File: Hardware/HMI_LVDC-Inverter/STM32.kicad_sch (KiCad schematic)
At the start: 22 parts, among them SW1 SW_MEC_5E, U4 STM32F103C8Tx, Y1 Crystal 8MHz

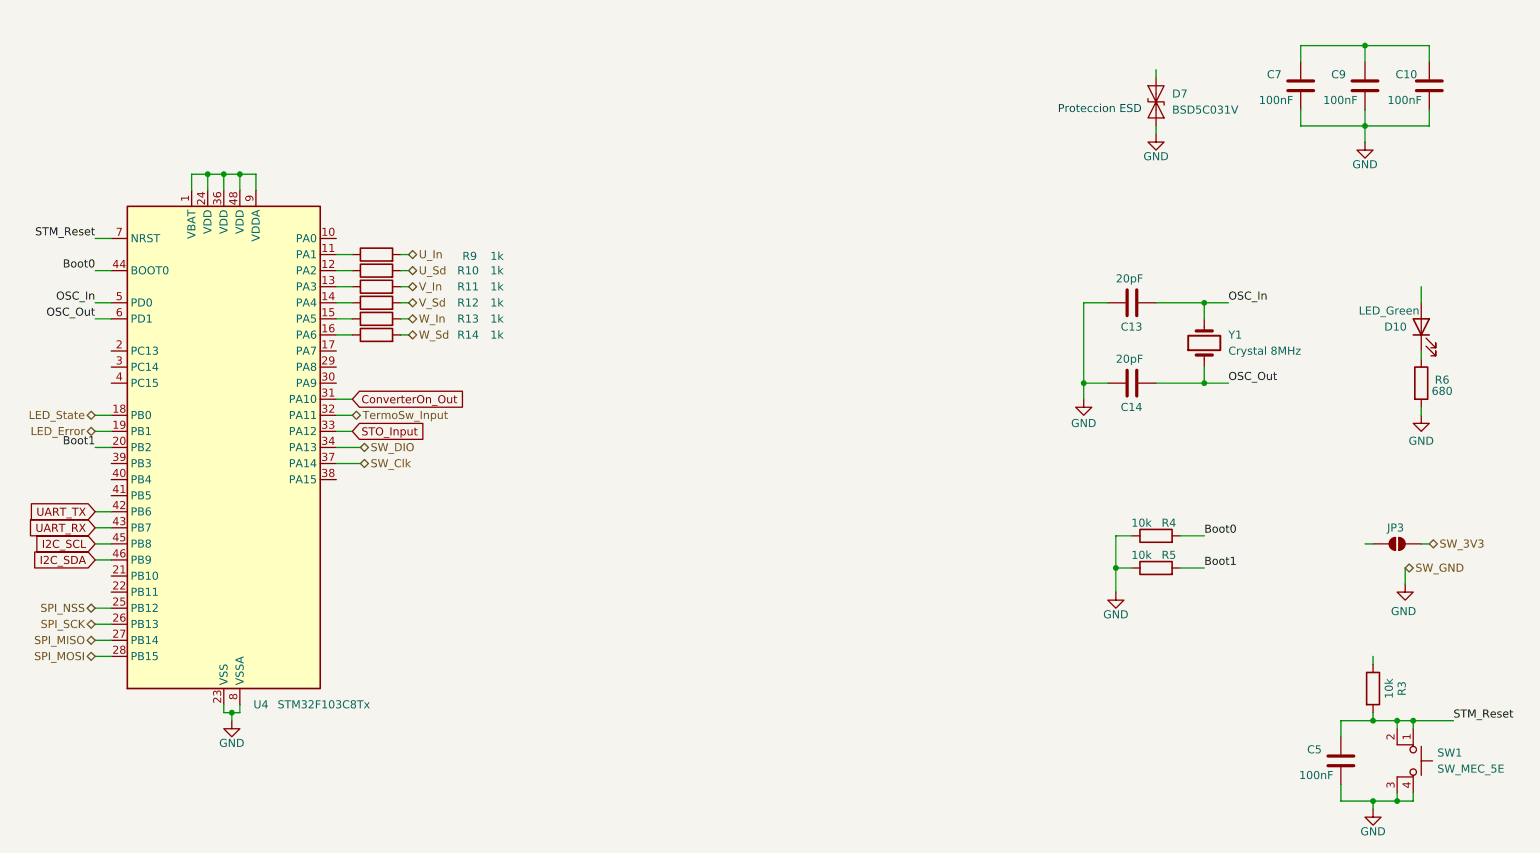
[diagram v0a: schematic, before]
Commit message: Terminado todo el conexionado eléctrico esquemático
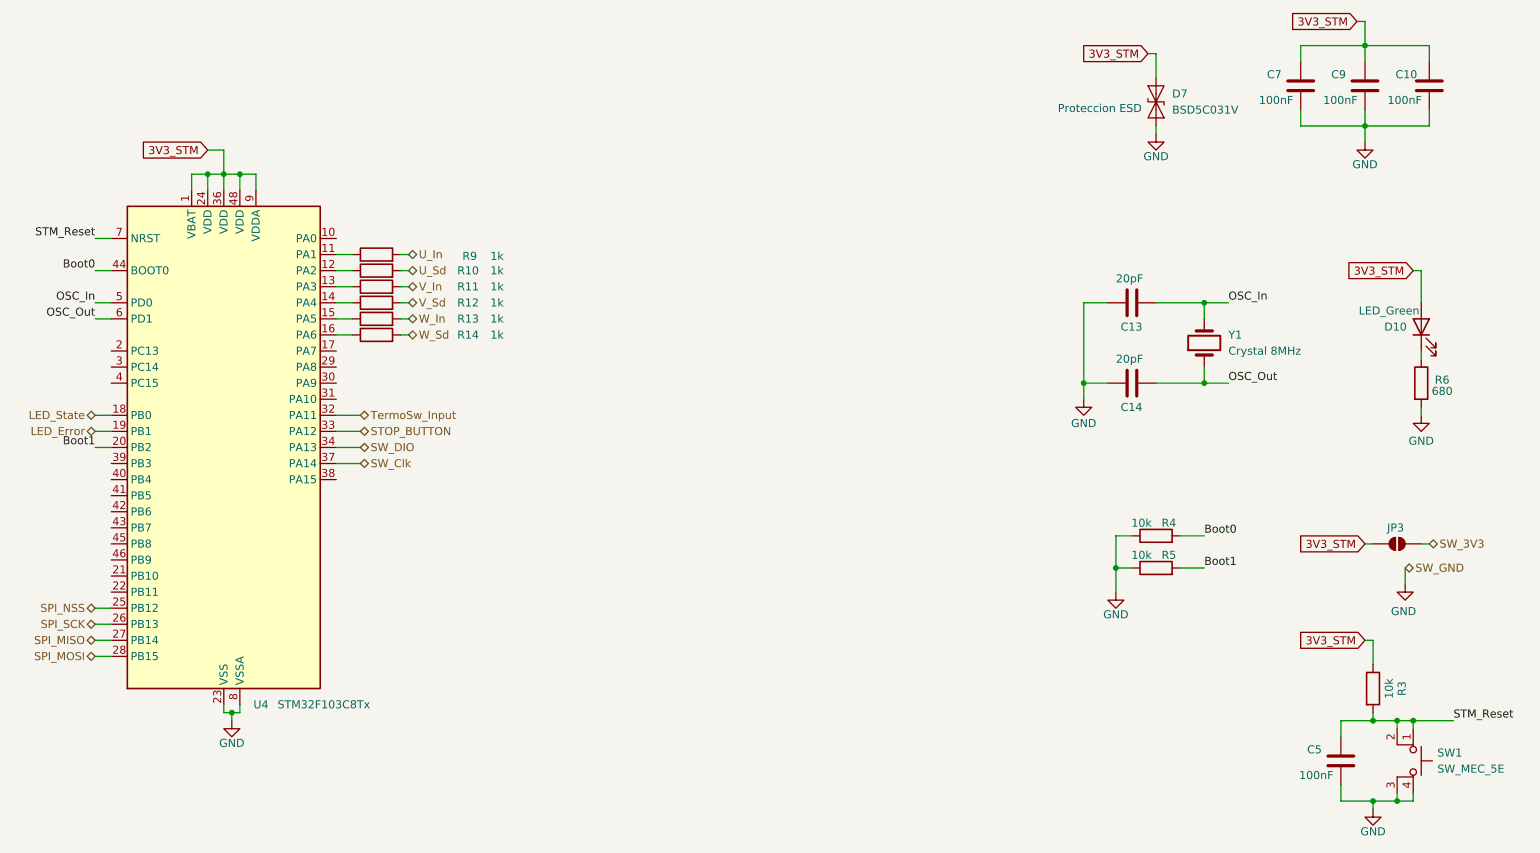
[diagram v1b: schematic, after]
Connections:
- net 3V3_STM: now reaches R3.1
- net 3V3_STM: now also C10.1, C7.1, C9.1, D10.2 (A), D7.2 (A2), JP3.1 (A), U4.1 (VBAT), U4.24 (VDD), U4.36 (VDD), U4.48 (VDD), U4.9 (VDDA)
- net ConverterOn_Out: no longer names the net of U4.31 (PA10)
- net I2C_SCL: no longer names the net of U4.45 (PB8)
- net I2C_SDA: no longer names the net of U4.46 (PB9)
- net STO_Input renamed STOP_BUTTON
- net UART_RX: no longer names the net of U4.43 (PB7)
- net UART_TX: no longer names the net of U4.42 (PB6)
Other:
- company: (none) -> Andrenacci - Carra
- title: (none) -> Variador de frecuencia LVDC

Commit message: Agregado de los componentes con links de compra en KiCAD a excepción de los conectores
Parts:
- removed SW1: SW_MEC_5E, TatilSwitch:Vertical SPST SMD Tactile Switches, symbol Switch:SW_MEC_5E
- added SW1: SolderJumper_2_Open, Jumper:SolderJumper-2_P1.3mm_Open_RoundedPad1.0x1.5mm, symbol Jumper:SolderJumper_2_Open
- C1: renamed from C7; Compra (none) -> https://www.lcsc.com/product-detail/C14663.html; Footprint checked (none) -> Yes; Manufacturer (none) -> Yagueo; Price (none) -> 0.24; Symbol checked (none) -> Yes
- C2: renamed from C9; Compra (none) -> https://www.lcsc.com/product-detail/C14663.html; Footprint checked (none) -> Yes; Manufacturer (none) -> Yagueo; Price (none) -> 0.24; Symbol checked (none) -> Yes
- C3: renamed from C10; Compra (none) -> https://www.lcsc.com/product-detail/C14663.html; Footprint checked (none) -> Yes; Manufacturer (none) -> Yagueo; Price (none) -> 0.24; Symbol checked (none) -> Yes
- C4: renamed from C13; Compra (none) -> https://www.lcsc.com/product-detail/C326779.html; Footprint checked (none) -> Yes; Manufacturer (none) -> Yagueo; Symbol checked (none) -> Yes
- C5: renamed from C14; Compra (none) -> https://www.lcsc.com/product-detail/C326779.html; Footprint checked (none) -> Yes; Manufacturer (none) -> Yagueo; Symbol checked (none) -> Yes
- C6: renamed from C5; Compra (none) -> https://www.lcsc.com/product-detail/C14663.html; Footprint checked (none) -> Yes; Manufacturer (none) -> Yagueo; Price (none) -> 0.24; Symbol checked (none) -> Yes
- D1: renamed from D7; Compra (none) -> https://www.lcsc.com/product-detail/C151984.html; Footprint checked (none) -> Yes; Manufacturer (none) -> Born; Price (none) -> 0.0284; Symbol checked (none) -> Yes
- D2: renamed from D10; Compra (none) -> https://www.lcsc.com/product-detail/C965804.html?s_z=n_XL-1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; Footprint checked (none) -> Yes; Manufacturer (none) -> XINGLIGHT; Price (none) -> 0.0044; Symbol checked (none) -> Yes
- R1: renamed from R9; value 1k -> 1K; Compra (none) -> https://www.lcsc.com/product-detail/C2653986.html; Footprint checked (none) -> Yes; Manufacturer (none) -> ROHM; Price (none) -> 0.0123; Symbol checked (none) -> Yes
- R10: renamed from R3; value 10k -> 10K; Compra (none) -> https://www.lcsc.com/product-detail/C491211.html; Footprint checked (none) -> Yes; Manufacturer (none) -> PANASONIC; Price (none) -> 0.0321; Symbol checked (none) -> Yes
- R2: renamed from R10; value 1k -> 1K; Compra (none) -> https://www.lcsc.com/product-detail/C2653986.html; Footprint checked (none) -> Yes; Manufacturer (none) -> ROHM; Price (none) -> 0.0123; Symbol checked (none) -> Yes
- R3: renamed from R11; value 1k -> 1K; Compra (none) -> https://www.lcsc.com/product-detail/C2653986.html; Footprint checked (none) -> Yes; Manufacturer (none) -> ROHM; Price (none) -> 0.0123; Symbol checked (none) -> Yes
- R4: renamed from R12; value 1k -> 1K; Compra (none) -> https://www.lcsc.com/product-detail/C2653986.html; Footprint checked (none) -> Yes; Manufacturer (none) -> ROHM; Price (none) -> 0.0123; Symbol checked (none) -> Yes
- R5: renamed from R13; value 1k -> 1K; Compra (none) -> https://www.lcsc.com/product-detail/C2653986.html; Footprint checked (none) -> Yes; Manufacturer (none) -> ROHM; Price (none) -> 0.0123; Symbol checked (none) -> Yes
- R6: renamed from R14; value 1k -> 1K; Compra (none) -> https://www.lcsc.com/product-detail/C2653986.html; Footprint checked (none) -> Yes; Manufacturer (none) -> ROHM; Price (none) -> 0.0123; Symbol checked (none) -> Yes
- R7: renamed from R6; Compra (none) -> https://www.lcsc.com/product-detail/C20109434.html; Footprint checked (none) -> Yes; Manufacturer (none) -> ROHM; Price (none) -> 0.0186; Symbol checked (none) -> Yes
- R8: renamed from R4; value 10k -> 10K; Compra (none) -> https://www.lcsc.com/product-detail/C491211.html; Footprint checked (none) -> Yes; Manufacturer (none) -> PANASONIC; Price (none) -> 0.0321; Symbol checked (none) -> Yes
- R9: renamed from R5; value 10k -> 10K; Compra (none) -> https://www.lcsc.com/product-detail/C491211.html; Footprint checked (none) -> Yes; Manufacturer (none) -> PANASONIC; Price (none) -> 0.0321; Symbol checked (none) -> Yes
- U1: renamed from U4; Compra (none) -> https://www.lcsc.com/product-detail/C8734.html?s_z=n_STM32F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; Manufacturer (none) -> ST; Price (none) -> 1.0546
- Y1: Compra (none) -> https://www.lcsc.com/product-detail/C12674.html; Footprint checked (none) -> Yes; Manufacturer (none) -> YXC Crystal Oscillators; Price (none) -> 0.0871; Symbol checked (none) -> Yes
- renumbered JP3 to JP1
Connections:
- net GND: now also SW1.1 (A)
- net STM_Reset: now also SW1.2 (B)
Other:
- moved on the sheet: C6

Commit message: Falta resolver los pulsadores
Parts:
- Y1: footprint Crystal:Crystal_SMD_HC49-SD -> Crystal:Crystal_SMD_0603-2Pin_6.0x3.5mm
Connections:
- no-connect marks 0 -> 18
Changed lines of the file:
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@@
 		(color 0 0 0 0)
 	)
+	(no_connect
+		(at 57.15 74.93)
+	)
+	(no_connect
+		(at 57.15 92.71)
+	)
+	(no_connect
+		(at 92.71 57.15)
+	)
+	(no_connect
+		(at 57.15 80.01)
+	)
+	(no_connect
+		(at 57.15 95.25)
+	)
+	(no_connect
+		(at 57.15 102.87)
+	)
+	(no_connect
+		(at 92.71 82.55)
+	)
+	(no_connect
+		(at 57.15 110.49)
+	)
+	(no_connect
+		(at 57.15 107.95)
+	)
+	(no_connect
+		(at 92.71 95.25)
+	)
+	(no_connect
+		(at 92.71 77.47)
+	)
+	(no_connect
+		(at 57.15 77.47)
+	)
+	(no_connect
+		(at 57.15 113.03)
+	)
+	(no_connect
+		(at 57.15 97.79)
+	)
+	(no_connect
+		(at 92.71 74.93)
+	)
+	(no_connect
+		(at 57.15 100.33)
+	)
+	(no_connect
+		(at 57.15 105.41)
+	)
+	(no_connect
+		(at 92.71 80.01)
+	)
 	(wire
 		(pts
@@
 			)
 		)
-		(property "Footprint" "Crystal:Crystal_SMD_HC49-SD"
+		(property "Footprint" "Crystal:Crystal_SMD_0603-2Pin_6.0x3.5mm"
 			(at 229.87 73.66 0)
 			(effects

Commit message: Agregado y corrección de borneras
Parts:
- Y1: footprint Crystal:Crystal_SMD_0603-2Pin_6.0x3.5mm -> Crystal:Crystal_SMD_5032-2Pin_5.0x3.2mm; Compra https://www.lcsc.com/product-detail/C12674.html -> https://www.lcsc.com/product-detail/C115962.html; Price 0.0871 -> 0.2002
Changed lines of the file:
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@@
 			)
 		)
+		(property "Sim.Library" ""
+			(at 99.06 64.77 90)
+			(effects
+				(font
+					(size 1.27 1.27)
+				)
+				(hide yes)
+			)
+		)
 		(pin "1"
 		)
@@
 			)
 		)
+		(property "Sim.Library" ""
+			(at 256.54 128.27 90)
+			(effects
+				(font
+					(size 1.27 1.27)
+				)
+				(hide yes)
+			)
+		)
 		(pin "1"
 		)
@@
 			)
 		)
+		(property "Sim.Library" ""
+			(at 218.44 80.01 90)
+			(effects
+				(font
+					(size 1.27 1.27)
+				)
+				(hide yes)
+			)
+		)
 		(pin "1"
 		)
@@
 			)
 		)
+		(property "Sim.Library" ""
+			(at 264.16 80.01 0)
+			(effects
+				(font
+					(size 1.27 1.27)
+				)
+				(hide yes)
+			)
+		)
 		(pin "1"
 		)
@@
 			)
 		)
+		(property "Sim.Library" ""
+			(at 222.25 109.22 90)
+			(effects
+				(font
+					(size 1.27 1.27)
+				)
+				(hide yes)
+			)
+		)
 		(pin "1"
 		)
@@
 			)
 		)
+		(property "Sim.Library" ""
+			(at 74.93 90.17 0)
+			(effects
+				(font
+					(size 1.27 1.27)
+				)
+				(hide yes)
+			)
+		)
 		(pin "11"
 		)
@@
 			)
 		)
+		(property "Sim.Library" ""
+			(at 261.62 139.7 90)
+			(effects
+				(font
+					(size 1.27 1.27)
+				)
+				(hide yes)
+			)
+		)
 		(pin "1"
 		)
@@
 			)
 		)
+		(property "Sim.Library" ""
+			(at 99.06 67.31 90)
+			(effects
+				(font
+					(size 1.27 1.27)
+				)
+				(hide yes)
+			)
+		)
 		(pin "1"
 		)
@@
 			)
 		)
+		(property "Sim.Library" ""
+			(at 99.06 69.85 90)
+			(effects
+				(font
+					(size 1.27 1.27)
+				)
+				(hide yes)
+			)
+		)
 		(pin "1"
 		)
@@
 			)
 		)
+		(property "Sim.Library" ""
+			(at 245.11 33.02 0)
+			(effects
+				(font
+					(size 1.27 1.27)
+				)
+				(hide yes)
+			)
+		)
 		(pin "1"
 		)
@@
 			)
 		)
+		(property "Sim.Library" ""
+			(at 256.54 139.7 0)
+			(effects
+				(font
+					(size 1.27 1.27)
+				)
+				(hide yes)
+			)
+		)
 		(pin "1"
 		)
@@
 			)
 		)
+		(property "Sim.Library" ""
+			(at 255.27 33.02 0)
+			(effects
+				(font
+					(size 1.27 1.27)
+				)
+				(hide yes)
+			)
+		)
 		(pin "1"
 		)
@@
 			)
 		)
+		(property "Sim.Library" ""
+			(at 222.25 104.14 90)
+			(effects
+				(font
+					(size 1.27 1.27)
+				)
+				(hide yes)
+			)
+		)
 		(pin "1"
 		)
@@
 			)
 		)
+		(property "Sim.Library" ""
+			(at 99.06 62.23 90)
+			(effects
+				(font
+					(size 1.27 1.27)
+				)
+				(hide yes)
+			)
+		)
 		(pin "1"
 		)
@@
 			)
 		)
+		(property "Sim.Library" ""
+			(at 218.44 67.31 90)
+			(effects
+				(font
+					(size 1.27 1.27)
+				)
+				(hide yes)
+			)
+		)
 		(pin "1"
 		)
@@
 			)
 		)
+		(property "Sim.Library" ""
+			(at 99.06 72.39 90)
+			(effects
+				(font
+					(size 1.27 1.27)
+				)
+				(hide yes)
+			)
+		)
 		(pin "1"
 		)
@@
 			)
 		)
-		(property "Footprint" "Crystal:Crystal_SMD_0603-2Pin_6.0x3.5mm"
+		(property "Footprint" "Crystal:Crystal_SMD_5032-2Pin_5.0x3.2mm"
 			(at 229.87 73.66 0)
 			(effects
@@
 			)
 		)
-		(property "Datasheet" "https://www.lcsc.com/datasheet/C12674.pdf"
+		(property "Datasheet" "https://www.lcsc.com/datasheet/C115962.pdf"
 			(at 229.87 73.66 0)
 			(effects
@@
 			)
 		)
-		(property "Compra" "https://www.lcsc.com/product-detail/C12674.html"
+		(property "Compra" "https://www.lcsc.com/product-detail/C115962.html"
 			(at 229.87 73.66 90)
 			(effects
@@
 			)
 		)
-		(property "Price" "0.0871"
+		(property "Price" "0.2002"
 			(at 229.87 73.66 90)
 			(effects
@@
 			)
 		)
+		(property "Sim.Library" ""
+			(at 229.87 73.66 90)
+			(effects
+				(font
+					(size 1.27 1.27)
+				)
+				(hide yes)
+			)
+		)
 		(pin "2"
 		)
@@
 			)
 		)
+		(property "Sim.Library" ""
+			(at 99.06 59.69 90)
+			(effects
+				(font
+					(size 1.27 1.27)
+				)
+				(hide yes)
+			)
+		)
 		(pin "1"
 		)
@@
 		(at 264.16 71.12 90)
 		(unit 1)
-		(exclude_from_sim no)
+		(exclude_from_sim yes)
 		(in_bom yes)
 		(on_board yes)
@@
 			)
 		)
+		(property "Sim.Library" ""
+			(at 264.16 71.12 90)
+			(effects
+				(font
+					(size 1.27 1.27)
+				)
+				(hide yes)
+			)
+		)
 		(pin "1"
 		)
@@
 			)
 		)
+		(property "Sim.Library" ""
+			(at 260.35 105.41 0)
+			(effects
+				(font
+					(size 1.27 1.27)
+				)
+				(hide yes)
+			)
+		)
 		(pin "1"
 		)
@@
 			)
 		)
+		(property "Sim.Library" ""
+			(at 265.43 33.02 0)
+			(effects
+				(font
+					(size 1.27 1.27)
+				)
+				(hide yes)
+			)
+		)
 		(pin "1"
 		)
@@
 			(at 222.25 35.56 90)
 			(effects
+				(font
+					(size 1.27 1.27)
+				)
+				(hide yes)
+			)
+		)
+		(property "Sim.Library" ""
+			(at 222.25 35.56 90)
+			(effects
